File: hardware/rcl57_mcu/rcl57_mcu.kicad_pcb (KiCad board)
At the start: 4 copper layers, 18 x 37 mm, 25 parts, among them J1 TMC1500 p1-13, J2 TMC1500 p28-16, J3 STLINK, Q1 DMP2240UDM-7, Q2 DMP2240UDM-7, Q3 DMP2240UDM-7, Q4 DMP2240UDM-7, U1 STM32F103TBUx, U2 TLC5929PWP, U3 TLV70033, U4 11AA080/TT

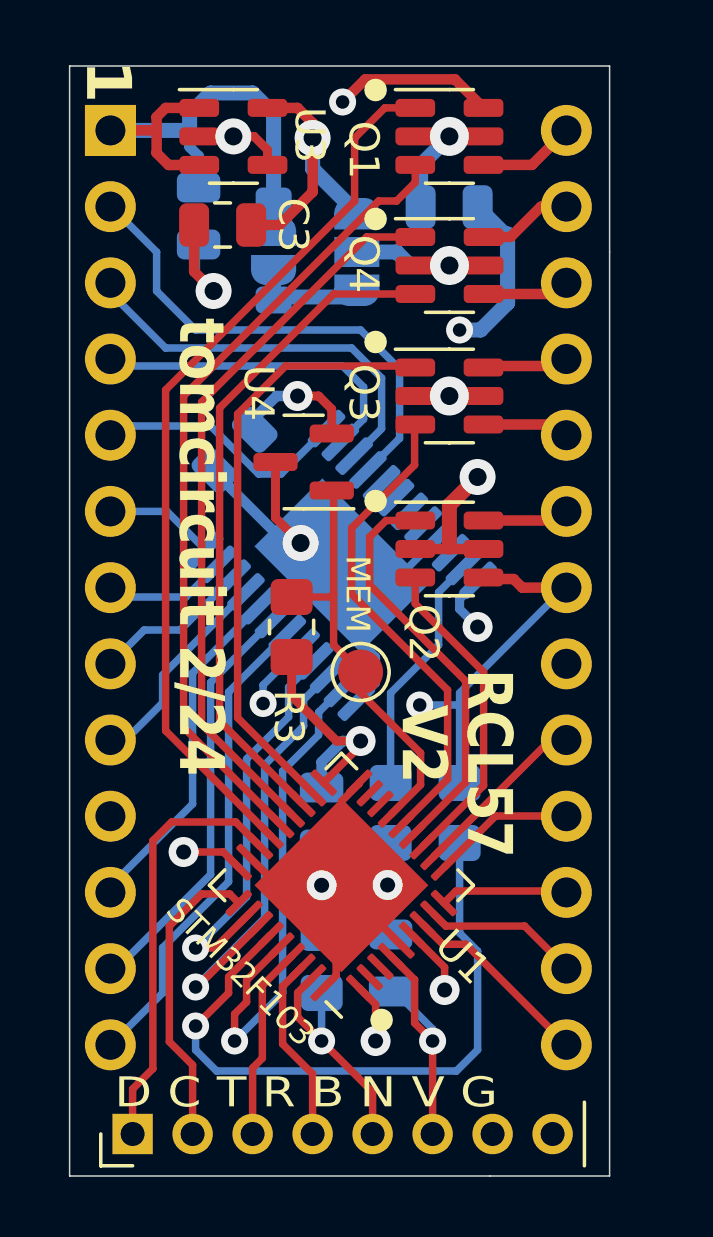
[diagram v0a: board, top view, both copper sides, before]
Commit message: working on TI55 donor board
ADC key column read, UNIO EEPROM read/init, power-save mode. Assumes V2 PCB with 2K pulldowns on K1-K5 inputs.

Updated schematic and PCB to "v3" to include the pulldown pack and simplify power options. V3 board not yet sent out for fabrication.
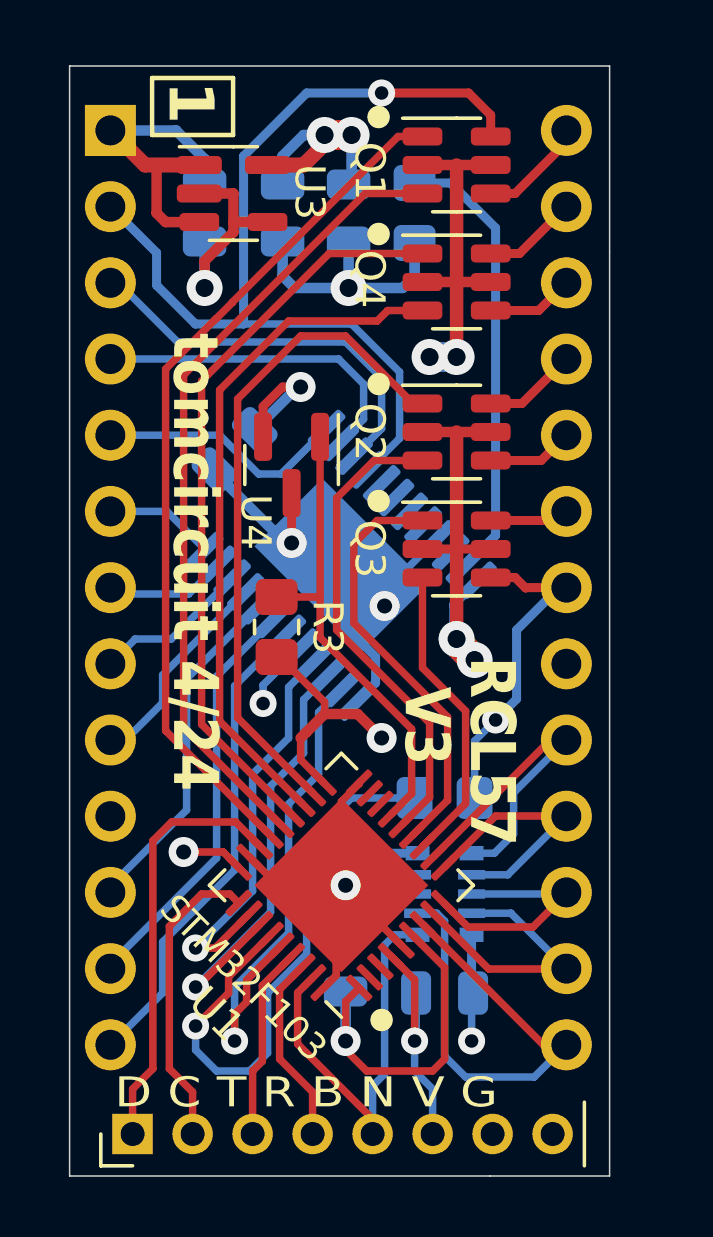
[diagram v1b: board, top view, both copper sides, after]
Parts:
- removed D2: MBR0520, Diode_SMD:D_SOD-123
- removed JP1: NoDiode, Jumper:SolderJumper-2_P1.3mm_Open_RoundedPad1.0x1.5mm
- removed JP2: VBUS, Jumper:SolderJumper-3_P1.3mm_Open_RoundedPad1.0x1.5mm_NumberLabels
- removed R2: 47K, Resistor_SMD:R_0805_2012Metric_Pad1.20x1.40mm_HandSolder
- removed TP1: MEMIO, TestPoint:TestPoint_Pad_D1.5mm
- added RN1: YC158TJR-072KL, Resistor_SMD:R_Array_Convex_5x0603, B.Cu at (148.3, 107.6)
- C3: moved to B.Cu
- R1: value 6.8K -> 2K
- R4: value 470 -> 330
- U3: value TLV70033 -> TLV70033_SOT23-5
- moved R1 20.0 mm to (147.3, 84.9)
- moved Q3 5.11 mm to (148.7, 96.1)
- moved C2 4.96 mm to (145.0, 109.9), turned to 90 degrees
- moved Q2 3.91 mm to (148.7, 92.2)
- moved C6 3.36 mm to (145.1, 84.9), turned to -90 degrees
- moved C1 2.06 mm to (148.3, 110.9), turned to 180 degrees
- moved C3 2.04 mm to (142.9, 84.9), turned to -90 degrees
- moved U3 1.90 mm to (141.3, 84.2)
- moved Q1 0.98 mm to (148.7, 83.3)
- moved R4 0.71 mm to (148.3, 104.4), turned to 180 degrees
- moved Q4 0.60 mm to (148.7, 87.2)
- moved R3 0.50 mm to (142.7, 98.7)
- moved U4 0.41 mm to (143.2, 93.3), turned to -90 degrees
- moved C5 0.22 mm to (140.3, 84.9)
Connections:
- net /D12MCU renamed /DIRECT
- C6 pad 1: VBUS -> +3V3
- Q1 pad 2: VBUS -> +3V3
- Q1 pad 5: VBUS -> +3V3
- Q2 pad 1: /A_DRIVE -> /C_DRIVE
- Q2 pad 2: VBUS -> +3V3
- Q2 pad 3: /D_DRIVE -> /B_DRIVE
- Q2 pad 4: /D12SD -> /SB
- Q2 pad 5: VBUS -> +3V3
- Q2 pad 6: /SA -> /SC
- Q3 pad 1: /C_DRIVE -> /A_DRIVE
- Q3 pad 2: VBUS -> +3V3
- Q3 pad 3: /B_DRIVE -> /D_DRIVE
- Q3 pad 4: /SB -> /D12SD
- Q3 pad 5: VBUS -> +3V3
- Q3 pad 6: /SC -> /SA
- Q4 pad 2: VBUS -> +3V3
- Q4 pad 5: VBUS -> +3V3
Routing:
- net VBUS: track 32.2 -> 0.00 mm, vias 4 -> 0
- net +3V3: track 36.5 -> 65.8 mm, vias 7 -> 10
- net /K1: track 6.45 -> 16.8 mm
- net +BATT: track 18.4 -> 11.0 mm
- net Net-(U2-IREF): track 8.22 -> 15.0 mm
- net /BOOT0: track 8.07 -> 14.2 mm, vias 1 -> 0
- net /K5: track 6.05 -> 11.9 mm
- net /K2: track 5.21 -> 9.21 mm
- net /K4: track 4.79 -> 8.76 mm
- net /K3: track 4.31 -> 8.18 mm
- net Net-(D2-K): track 3.82 -> 0.00 mm
- net /DIRECT: track 22.0 -> 19.6 mm
- net /D12SD: track 19.9 -> 22.3 mm
- net /C_DRIVE: track 20.3 -> 22.1 mm
- net /MEMIO: track 13.9 -> 15.6 mm
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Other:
- board text added: "Digit Iset"
- board text added: "V3"
- board text added: "tomcircuit 4/24"
- board text removed: "Iset"
- board text removed: "K"
- board text removed: "V2"
- board text removed: "tomcircuit 2/24"
